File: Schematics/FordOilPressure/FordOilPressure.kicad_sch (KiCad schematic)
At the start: 14 parts

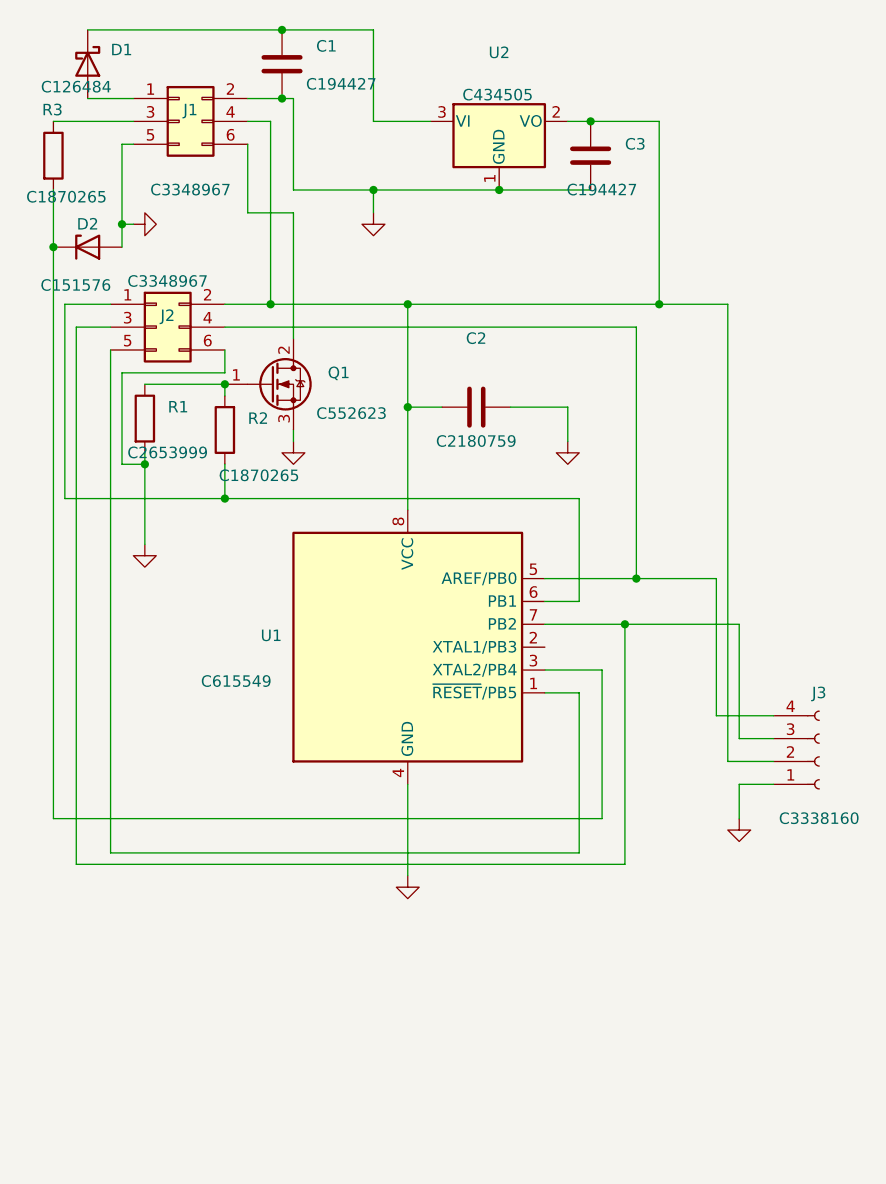
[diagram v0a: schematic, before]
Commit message: This is the latest with ATTiny1626
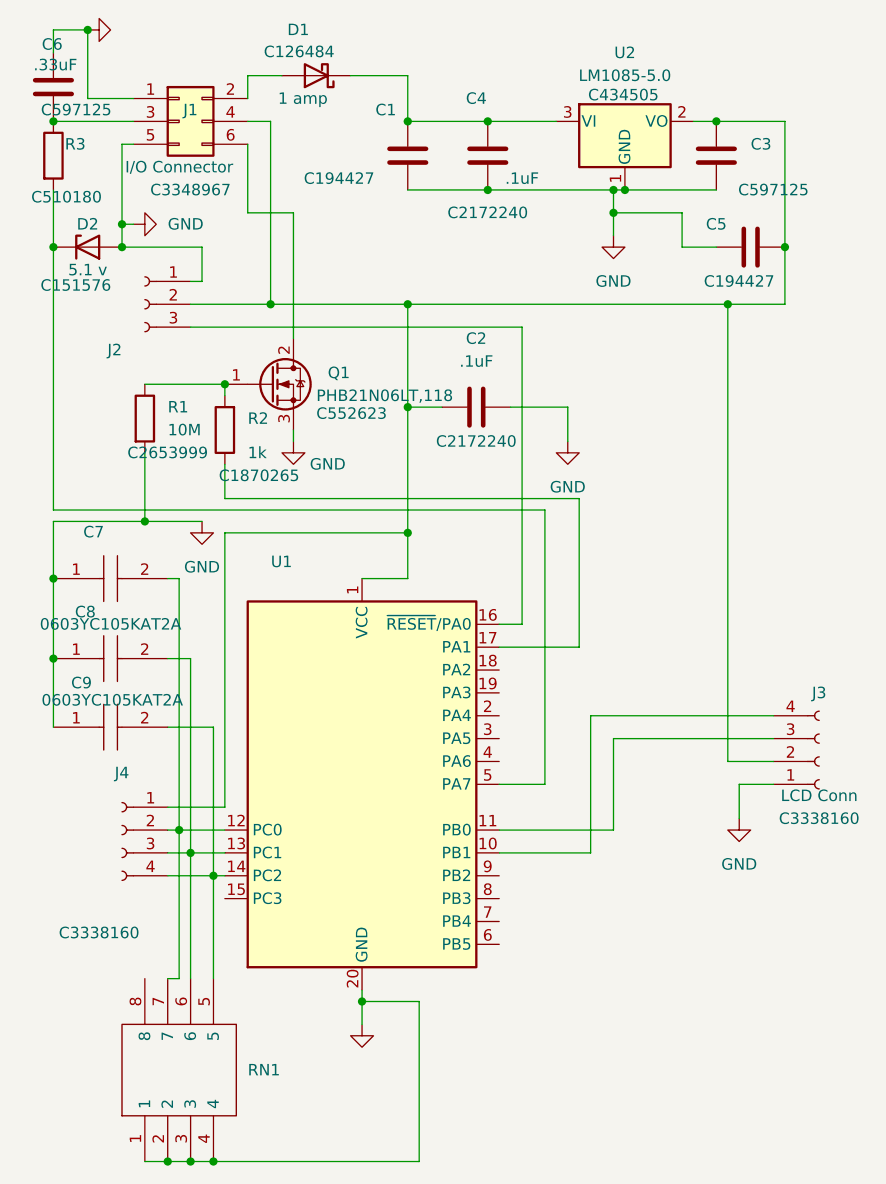
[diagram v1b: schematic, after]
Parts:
- removed J2: (no value), symbol Connector_Generic:Conn_02x03_Odd_Even
- removed U1: (no value), symbol MCU_Microchip_ATtiny:ATtiny85-20S
- added C4: .1uF, Capacitor_SMD:C_0603_1608Metric_Pad1.08x0.95mm_HandSolder, symbol Device:C
- added C5: (no value), symbol Device:C
- added C6: .33uF, Capacitor_SMD:C_0603_1608Metric_Pad1.08x0.95mm_HandSolder, symbol Device:C
- added C7: (no value), symbol SamacSys_Parts:0603YC105KAT2A
- added C8, C9: 0603YC105KAT2A, CAPC1608X94N, symbol SamacSys_Parts:0603YC105KAT2A
- added J2: (no value), symbol Connector:Conn_01x03_Female
- added J4: (no value), Connector_PinHeader_2.54mm:PinHeader_1x04_P2.54mm_Vertical, symbol Connector:Conn_01x04_Female
- added RN1: (no value), symbol SamacSys_Parts:EXBV8V683JV
- added U1: (no value), symbol MCU_Microchip_ATtiny:ATtiny1616-S
- C2: value (none) -> .1uF; footprint (none) -> Capacitor_SMD:C_0603_1608Metric_Pad1.08x0.95mm_HandSolder; LCSC C2180759 -> C2172240
- C3: LCSC C194427 -> C597125
- D1: value (none) -> 1 amp; footprint (none) -> Diode_SMD:D_SOD-123F
- D2: value (none) -> 5.1 v; footprint (none) -> Diode_SMD:D_SOD-123
- J1: value (none) -> I/O Connector; footprint (none) -> Connector_PinHeader_2.54mm:PinHeader_2x03_P2.54mm_Vertical
- J3: value (none) -> LCD Conn; footprint (none) -> Connector_PinHeader_2.54mm:PinHeader_1x04_P2.54mm_Vertical
- Q1: value (none) -> PHB21N06LT,118; footprint (none) -> Package_TO_SOT_SMD:TO-263-2
- R1: value (none) -> 10M; footprint (none) -> Resistor_SMD:R_0603_1608Metric_Pad0.98x0.95mm_HandSolder
- R2: value (none) -> 1k; footprint (none) -> Resistor_SMD:R_0603_1608Metric_Pad0.98x0.95mm_HandSolder
- R3: LCSC C1870265 -> C510180
- U2: value (none) -> LM1085-5.0; footprint (none) -> Package_TO_SOT_SMD:TO-263-3_TabPin2
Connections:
- net GND: now also C1.1, J1.1 (Pin_1), C4.2, C5.1, C6.1, C7.1, C8.1, C9.1, J2.1 (Pin_1), RN1.1, RN1.2, RN1.3, RN1.4, U1.20 (GND); no longer C1.2, J1.2 (Pin_2)
- net at C2.1, C3.1, J1.4 (Pin_4)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: now also C5.2, J2.2 (Pin_2), J4.1 (Pin_1), U1.1 (VCC)
- net at D1.1 (K), U2.3 (VI): now also C1.2, C4.1; no longer C1.1
- net at D1.2 (A): now also J1.2 (Pin_2); no longer J1.1 (Pin_1)
- net at J1.3 (Pin_3), R3.1: now also C6.2
- net at J3.3 (Pin_3): now also U1.11 (PB0)
- net at J3.4 (Pin_4): now also U1.10 (PB1)
- net at R2.1: now also U1.17 (PA1)
- net at D2.1 (K), R3.2: now also U1.5 (PA7)
- new net: J2.3 (Pin_3), U1.16 (~{RESET}/PA0)
- new net: C7.2, J4.2 (Pin_2), RN1.7, U1.12 (PC0)
- new net: C8.2, J4.3 (Pin_3), RN1.6, U1.13 (PC1)
- new net: C9.2, J4.4 (Pin_4), RN1.5, U1.14 (PC2)
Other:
- moved on the sheet: C1, C3, D1, U2
